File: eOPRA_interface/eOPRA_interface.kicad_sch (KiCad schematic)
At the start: 22 parts, among them J1 CONN_01X04_MALE, J2 CONN_01X04_MALE, J3 CONN_01X04_MALE, J4 CONN_01X02_MALE, J5 CONN_01X04_MALE, J6 CONN_02X10, J7 CONN_01X04_MALE, J8 CONN_01X04_MALE, Q5 Q_PMOS_GSD, U1 ARM-SWD-10, U10 USB_C_2.0, U27 Mounting-holes, U28 Mounting-holes, U5 XT-X, U7 Mounting-holes, U8 Mounting-holes

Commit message: stuffs
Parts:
- TP5: footprint 0_misc:test_point_0.8mm_square -> 0_misc:plated_hole_1.1x1.5mm
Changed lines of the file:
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@@
       (effects (font (size 1.27 1.27)))
     )
-    (property "Footprint" "0_misc:test_point_0.8mm_square" (at 88.265 194.31 0)
+    (property "Footprint" "0_misc:plated_hole_1.1x1.5mm" (at 88.265 194.31 0)
       (effects (font (size 1.27 1.27)) hide)
     )
@@
       (effects (font (size 1.27 1.27)))
     )
-    (property "Footprint" "0_misc:test_point_0.8mm_square" (at 88.265 187.96 0)
-      (effects (font (size 1.27 1.27)) hide)
-    )
+    (property "Footprint" "0_misc:plated_hole_1.1x1.5mm" (at 88.265 187.96 0)
+      (effects (font (size 1.27 1.27)) hide)
+    )

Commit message: initial state
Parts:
- D2: PN 3,2 -> 3,6
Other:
- sheet processor ports: added SWITCH_CTL; removed none
- sheet switch_control ports: added SWITCH_CTL; removed none
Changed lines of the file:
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@@
+    (stroke (width 0) (type default))
+  )
+  (wire (pts (xy 140.335 160.02) (xy 140.335 169.545))
     (stroke (width 0) (type default))
   )
@@
       (effects (font (size 1.27 1.27)) hide)
     )
-    (property "PN" "3,2" (at 120.015 56.515 0)
+    (property "PN" "3,6" (at 120.015 56.515 0)
       (effects (font (size 1.27 1.27)) hide)
     )
@@
       (effects (font (size 1.27 1.27)) (justify right))
     )
+    (pin "SWITCH_CTL" input (at 140.335 169.545 90)
+      (effects (font (size 1.27 1.27)) (justify right))
+    )
     (instances
       (project "eOPRA_interface"
@@
       (effects (font (size 1.27 1.27)) (justify right))
     )
-    (instances
+    (pin "SWITCH_CTL" output (at 140.335 160.02 270)
+      (effects (font (size 1.27 1.27)) (justify left))
+    )
+    (instances

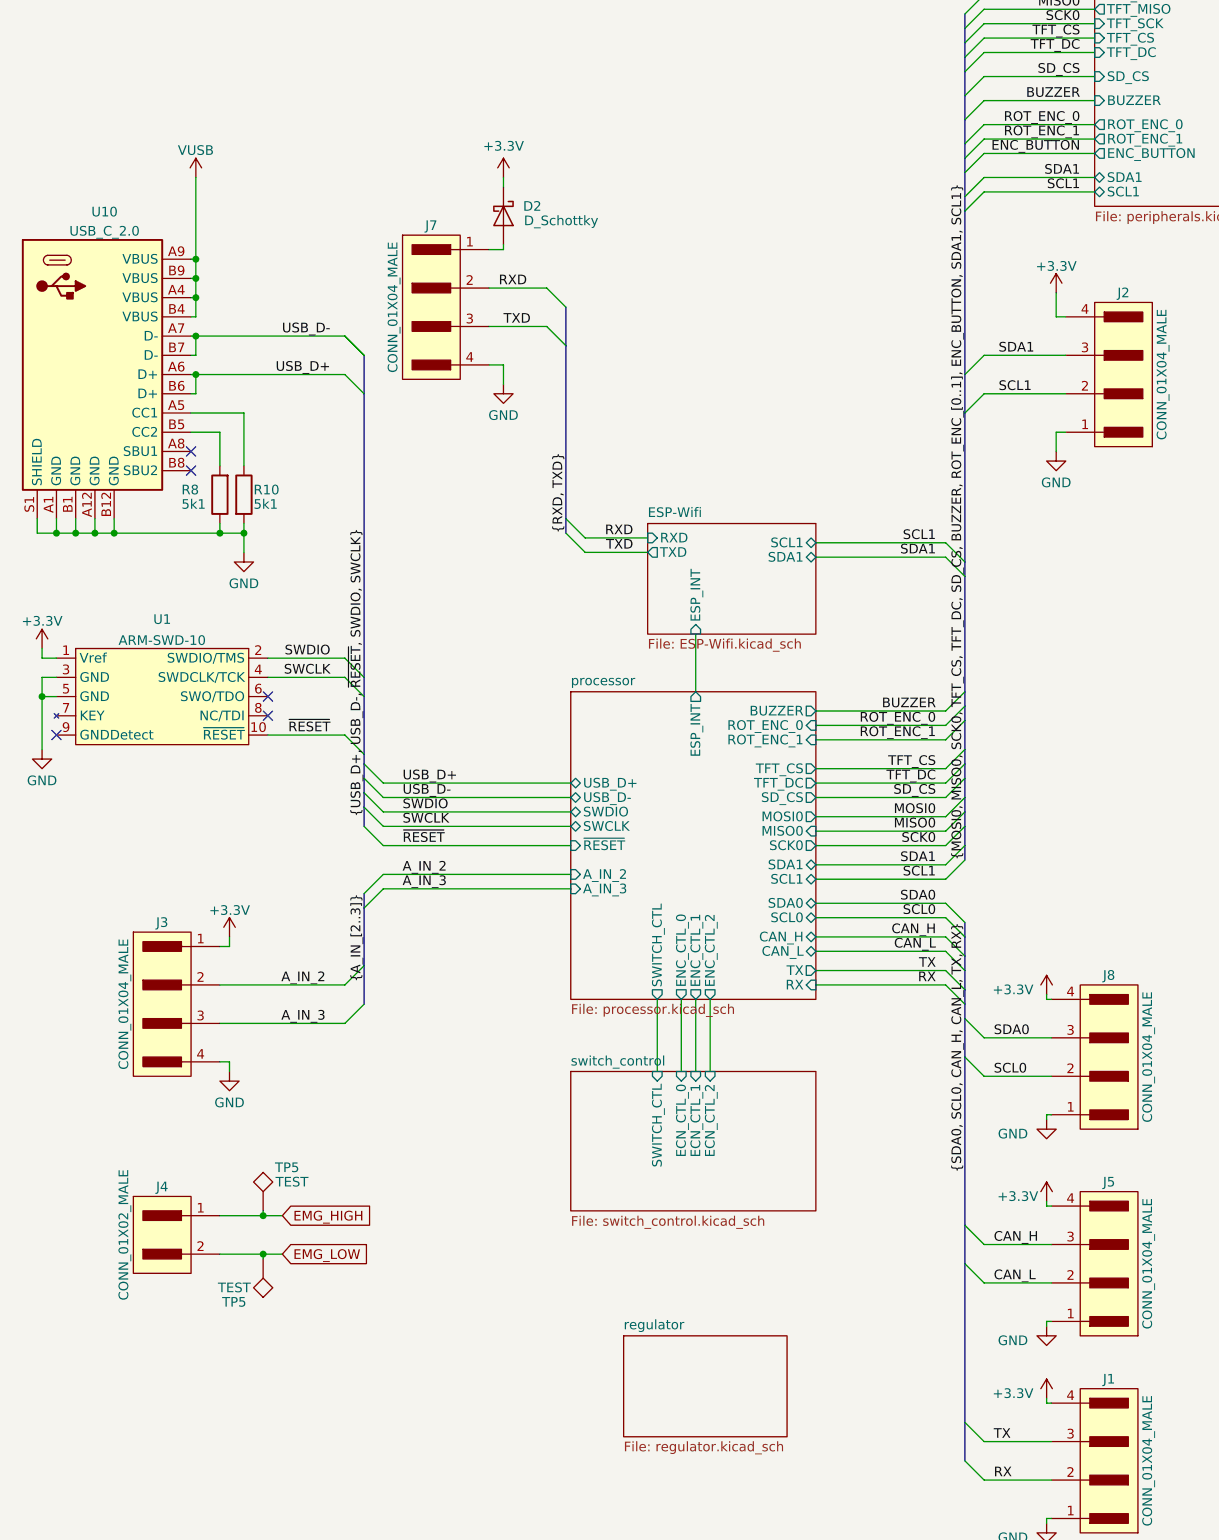
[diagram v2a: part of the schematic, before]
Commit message: switch port on interrupt
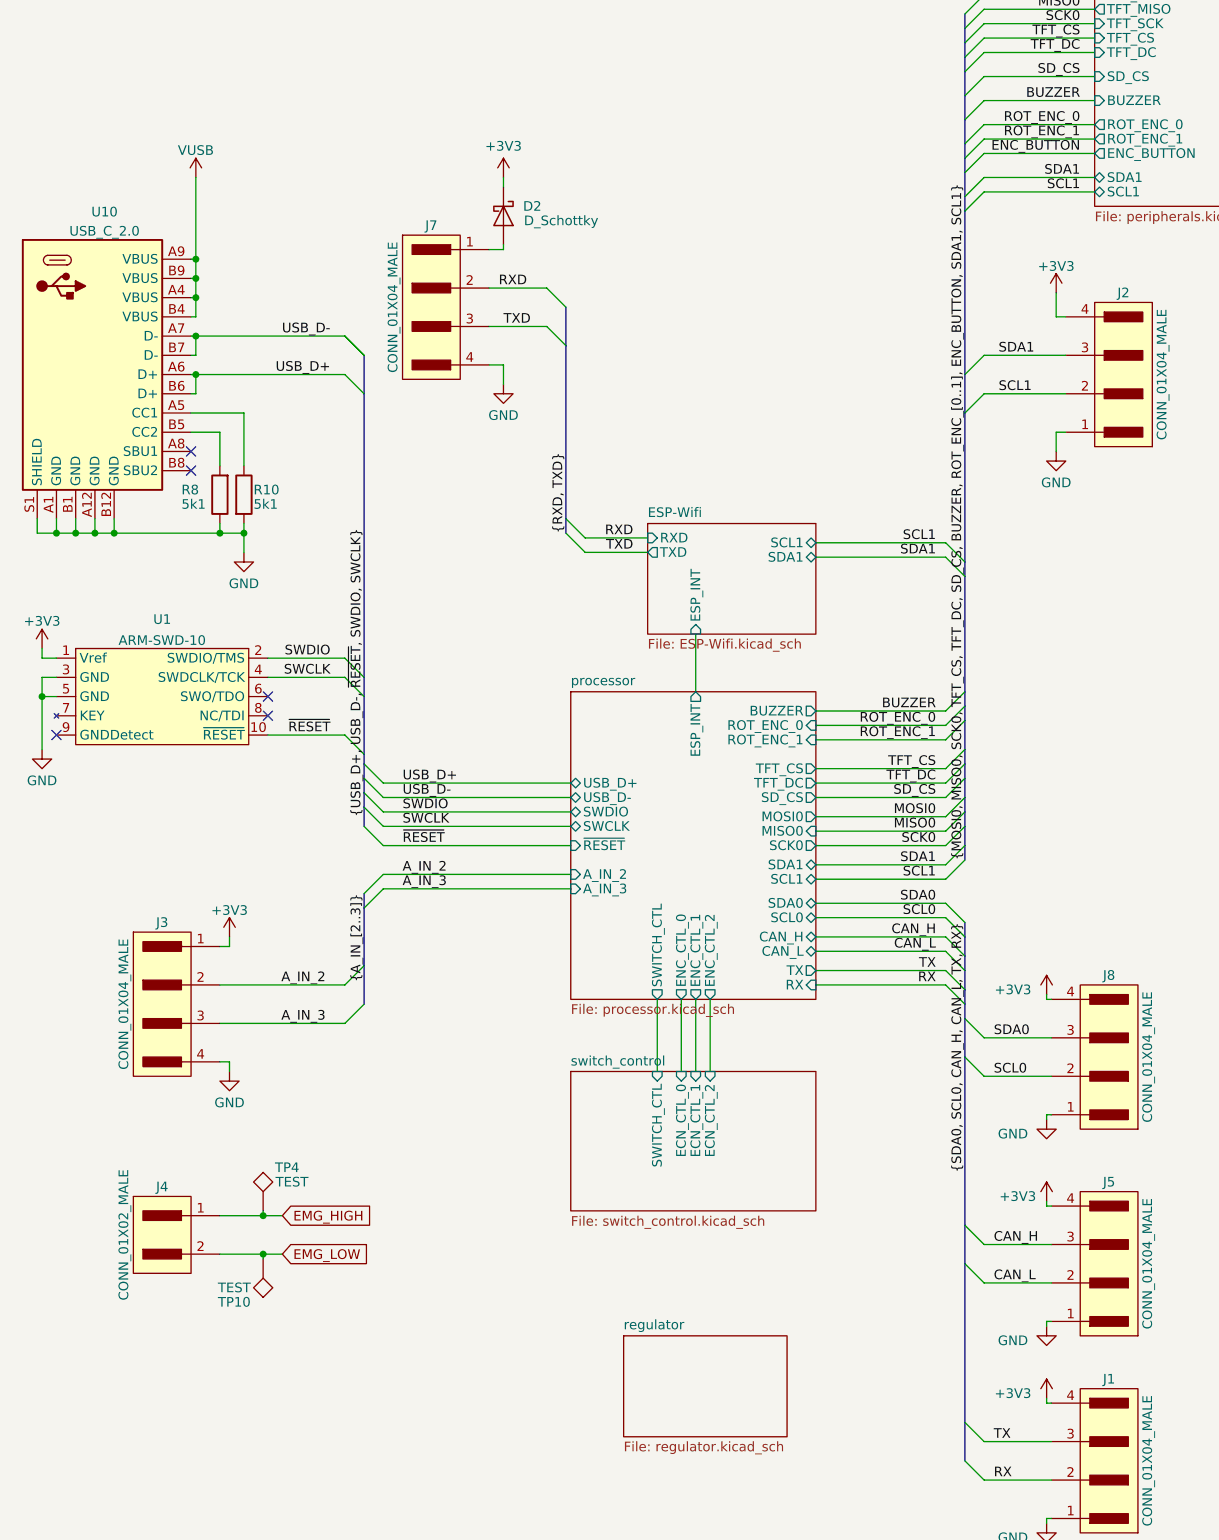
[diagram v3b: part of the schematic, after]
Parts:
- renumbered TP5 to TP10, TP5 to TP4
